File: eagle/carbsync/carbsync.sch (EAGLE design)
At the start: 27 parts, among them Q1 IRLML6344

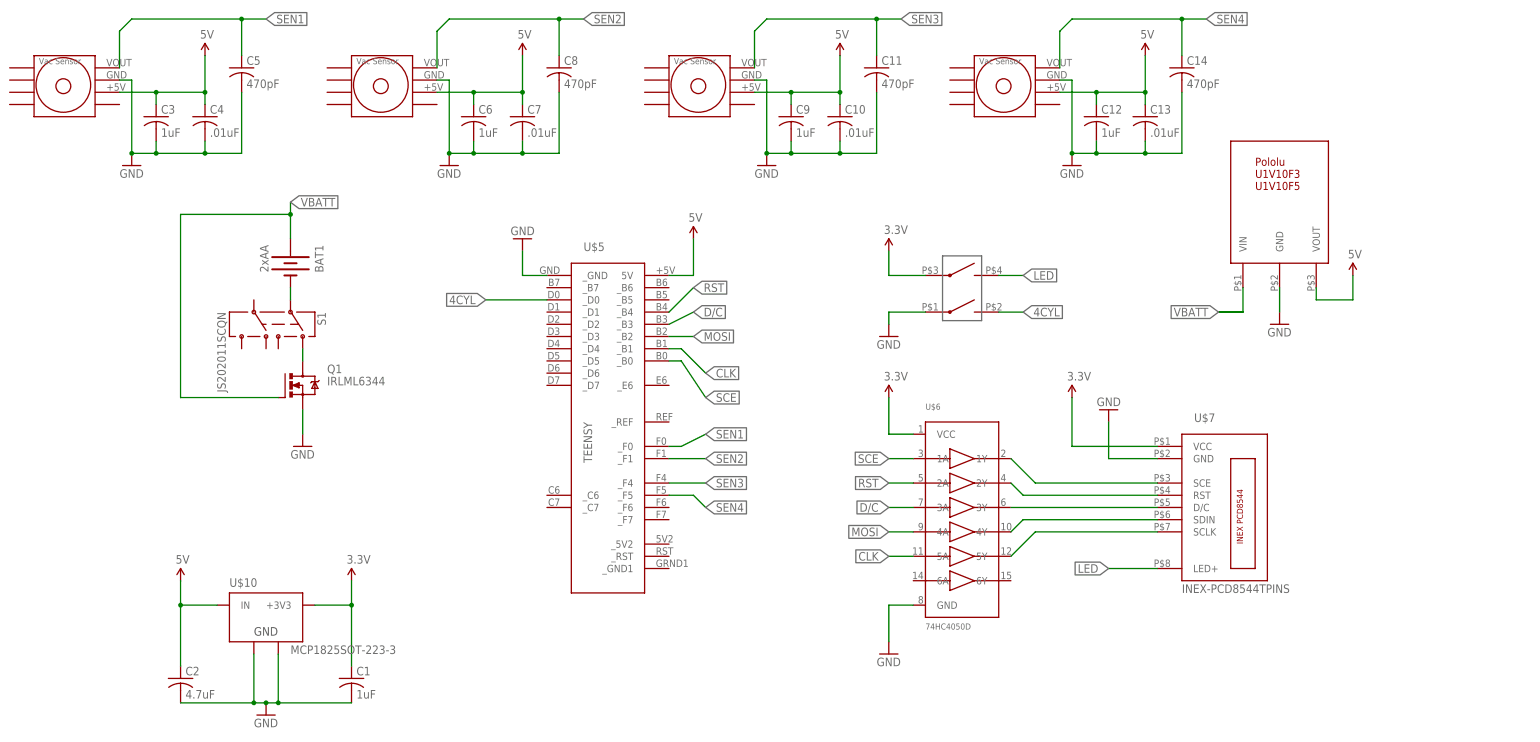
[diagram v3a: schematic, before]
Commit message: redesign PCB around http://www.hammondmfg.com/pdf/1553D_BAT.pdf
still need to find a power switch which will work correctly
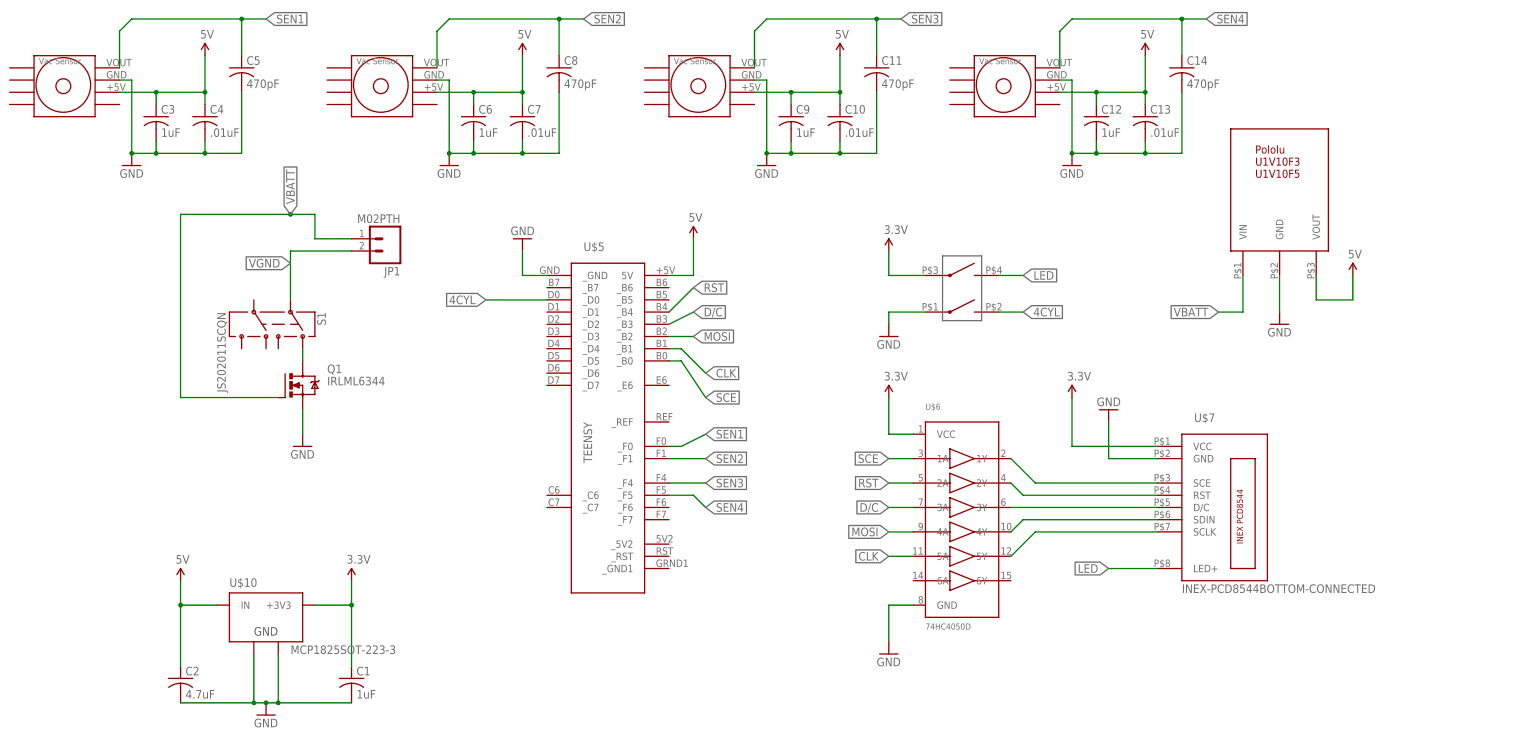
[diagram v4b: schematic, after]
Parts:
- removed BAT1: 2xAA, synfinatic:BATTERYKEYSTONE-2462-2-AA
- added JP1: M02PTH, SparkFun-Connectors:M02PTH
- U$7: value INEX-PCD8544TPINS -> INEX-PCD8544BOTTOM-CONNECTED; device synfinatic:INEX-PCD8544TPINS -> synfinatic:INEX-PCD8544BOTTOM-CONNECTED
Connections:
- removed net N$7: BAT1.-, S1.2
- new net VGND: JP1.2, S1.2
- net VBATT: now also JP1.1; no longer BAT1.+
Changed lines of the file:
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@@
 <layer number="111" name="LPC17xx" color="7" fill="1" visible="no" active="yes"/>
 <layer number="112" name="tSilk" color="7" fill="1" visible="no" active="yes"/>
+<layer number="113" name="IDFDebug" color="4" fill="1" visible="yes" active="yes"/>
 <layer number="116" name="Patch_BOT" color="9" fill="4" visible="no" active="yes"/>
 <layer number="121" name="_tsilk" color="7" fill="1" visible="yes" active="yes"/>
@@
 <part name="U$5" library="teensy" deviceset="TEENSY" device=""/>
 <part name="U$1" library="synfinatic" deviceset="MPXV5050V" device=""/>
-<part name="U$7" library="synfinatic" deviceset="INEX-PCD8544" device="TPINS" value="INEX-PCD8544TPINS"/>
+<part name="U$7" library="synfinatic" deviceset="INEX-PCD8544" device="BOTTOM-CONNECTED" value="INEX-PCD8544BOTTOM-CONNECTED"/>
 <part name="SUPPLY2" library="SparkFun-Aesthetics" deviceset="5V" device=""/>
 <part name="GND2" library="SparkFun-Aesthetics" deviceset="GND" device=""/>
@@
 <part name="C13" library="resistor" deviceset="C-US" device="C0805" value=".01uF"/>
 <part name="C14" library="resistor" deviceset="C-US" device="C0603" value="470pF"/>
-<part name="BAT1" library="synfinatic" deviceset="BATTERY" device="KEYSTONE-2462-2-AA" value="2xAA"/>
 <part name="U$9" library="synfinatic" deviceset="CT-219-X-MST" device=""/>
 <part name="SUPPLY10" library="SparkFun-Aesthetics" deviceset="3.3V" device=""/>
 <part name="GND12" library="SparkFun-Aesthetics" deviceset="GND" device=""/>
 <part name="Q1" library="synfinatic" deviceset="IRLML6344" device=""/>
+<part name="JP1" library="SparkFun-Connectors" deviceset="M02" device="PTH"/>
 </parts>
 <sheets>
@@
 <instance part="U$6" gate="G$1" x="111.76" y="38.1"/>
 <instance part="GND6" gate="1" x="96.52" y="10.16"/>
-<instance part="U$8" gate="G$1" x="167.64" y="91.44"/>
+<instance part="U$8" gate="G$1" x="167.64" y="93.98"/>
 <instance part="GND1" gate="1" x="177.8" y="78.74"/>
 <instance part="SUPPLY1" gate="G$1" x="193.04" y="88.9"/>
@@
 <instance part="C13" gate="G$1" x="149.86" y="121.92"/>
 <instance part="C14" gate="G$1" x="157.48" y="132.08"/>
-<instance part="BAT1" gate="G$1" x="-27.94" y="91.44" rot="R270"/>
 <instance part="U$9" gate="DIP$1" x="109.22" y="83.82"/>
 <instance part="SUPPLY10" gate="G$1" x="96.52" y="93.98"/>
 <instance part="GND12" gate="1" x="96.52" y="76.2"/>
 <instance part="Q1" gate="G$1" x="-27.94" y="66.04"/>
+<instance part="JP1" gate="G$1" x="-7.62" y="96.52" rot="R180"/>
 </instances>
 <busses>
@@
 <segment>
 <pinref part="U$8" gate="G$1" pin="GND"/>
-<wire x1="177.8" y1="86.36" x2="177.8" y2="81.28" width="0.1524" layer="91"/>
+<wire x1="177.8" y1="88.9" x2="177.8" y2="81.28" width="0.1524" layer="91"/>
 <pinref part="GND1" gate="1" pin="GND"/>
 </segment>
@@
 <segment>
 <pinref part="U$8" gate="G$1" pin="VOUT"/>
-<wire x1="185.42" y1="86.36" x2="185.42" y2="83.82" width="0.1524" layer="91"/>
+<wire x1="185.42" y1="88.9" x2="185.42" y2="83.82" width="0.1524" layer="91"/>
 <wire x1="185.42" y1="83.82" x2="193.04" y2="83.82" width="0.1524" layer="91"/>
 <wire x1="193.04" y1="83.82" x2="193.04" y2="88.9" width="0.1524" layer="91"/>
@@
 <net name="VBATT" class="0">
 <segment>
-<pinref part="U$8" gate="G$1" pin="VIN"/>
-<wire x1="170.18" y1="86.36" x2="170.18" y2="81.28" width="0.1524" layer="91"/>
-<wire x1="170.18" y1="81.28" x2="165.1" y2="81.28" width="0.1524" layer="91"/>
 <label x="165.1" y="81.28" size="1.778" layer="95" rot="R180" xref="yes"/>
 <wire x1="170.18" y1="81.28" x2="165.1" y2="81.28" width="0.1524" layer="91"/>
-</segment>
-<segment>
-<pinref part="BAT1" gate="G$1" pin="+"/>
-<wire x1="-27.94" y1="104.14" x2="-27.94" y2="101.6" width="0.1524" layer="91"/>
-<label x="-27.94" y="104.14" size="1.778" layer="95" xref="yes"/>
+<pinref part="U$8" gate="G$1" pin="VIN"/>
+<wire x1="170.18" y1="81.28" x2="170.18" y2="88.9" width="0.1524" layer="91"/>
+</segment>
+<segment>
+<label x="-27.94" y="101.6" size="1.778" layer="95" rot="R90" xref="yes"/>
 <pinref part="Q1" gate="G$1" pin="G"/>
-<wire x1="-27.94" y1="101.6" x2="-27.94" y2="96.52" width="0.1524" layer="91"/>
 <wire x1="-30.48" y1="63.5" x2="-50.8" y2="63.5" width="0.1524" layer="91"/>
 <wire x1="-50.8" y1="63.5" x2="-50.8" y2="101.6" width="0.1524" layer="91"/>
 <wire x1="-50.8" y1="101.6" x2="-27.94" y2="101.6" width="0.1524" layer="91"/>
+<wire x1="-27.94" y1="101.6" x2="-22.86" y2="101.6" width="0.1524" layer="91"/>
 <junction x="-27.94" y="101.6"/>
+<wire x1="-22.86" y1="101.6" x2="-22.86" y2="96.52" width="0.1524" layer="91"/>
+<pinref part="JP1" gate="G$1" pin="1"/>
+<wire x1="-15.24" y1="96.52" x2="-22.86" y2="96.52" width="0.1524" layer="91"/>
 </segment>
 </net>
@@
 </segment>
 </net>
-<net name="N$7" class="0">
-<segment>
-<pinref part="BAT1" gate="G$1" pin="-"/>
+<net name="VGND" class="0">
+<segment>
 <pinref part="S1" gate="G$1" pin="2"/>
-<wire x1="-27.94" y1="86.36" x2="-27.94" y2="83.82" width="0.1524" layer="91"/>
-</segment>
-</net>
+<wire x1="-27.94" y1="93.98" x2="-27.94" y2="83.82" width="0.1524" layer="91"/>
+<label x="-27.94" y="91.44" size="1.778" layer="95" rot="R180" xref="yes"/>
+<pinref part="JP1" gate="G$1" pin="2"/>
+<wire x1="-15.24" y1="93.98" x2="-27.94" y2="93.98" width="0.1524" layer="91"/>
+</segment>
+</net>

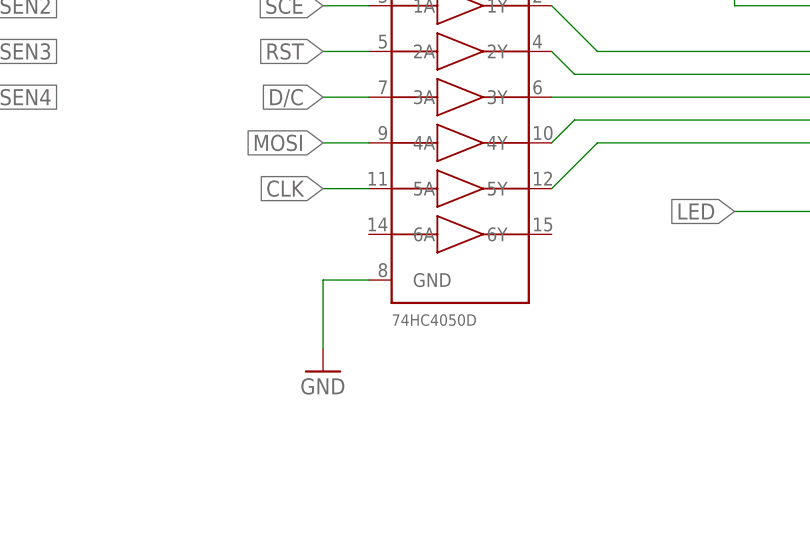
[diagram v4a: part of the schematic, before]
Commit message: clean up board and fix the level shifter
Waiting on part order to check footprints & do power switch
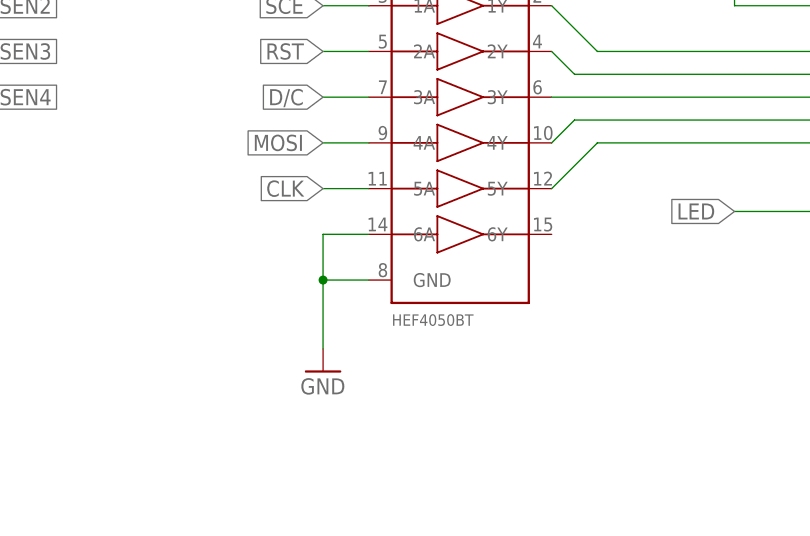
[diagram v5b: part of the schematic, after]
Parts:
- U$6: value 74HC4050D -> HEF4050BT
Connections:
- net GND: now also U$6.6A
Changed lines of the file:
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@@
 <part name="GND4" library="SparkFun-Aesthetics" deviceset="GND" device=""/>
 <part name="SUPPLY5" library="SparkFun-Aesthetics" deviceset="5V" device=""/>
-<part name="U$6" library="microbuilder" deviceset="74HC4050D" device="" value="74HC4050D"/>
+<part name="U$6" library="microbuilder" deviceset="74HC4050D" device="" value="HEF4050BT"/>
 <part name="GND6" library="SparkFun-Aesthetics" deviceset="GND" device=""/>
 <part name="U$8" library="synfinatic" deviceset="POLOLU-DC-3PIN" device="U1V10F5-5V-DC-UP"/>
@@
 <wire x1="96.52" y1="20.32" x2="96.52" y2="12.7" width="0.1524" layer="91"/>
 <pinref part="GND6" gate="1" pin="GND"/>
+<pinref part="U$6" gate="G$1" pin="6A"/>
+<wire x1="101.6" y1="25.4" x2="96.52" y2="25.4" width="0.1524" layer="91"/>
+<wire x1="96.52" y1="25.4" x2="96.52" y2="20.32" width="0.1524" layer="91"/>
+<junction x="96.52" y="20.32"/>
 </segment>
 <segment>

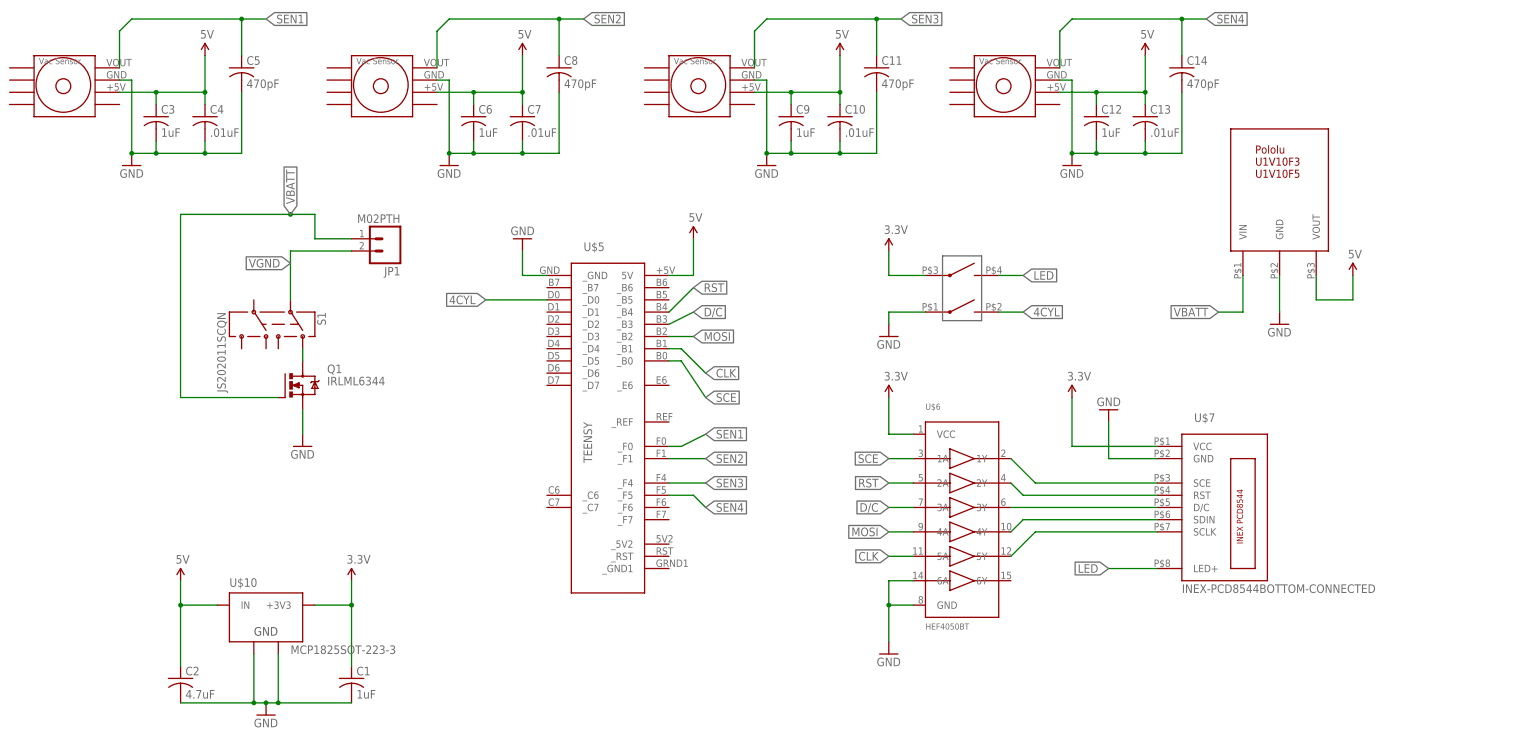
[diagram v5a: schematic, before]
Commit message: v1.0 of PCB done and ordered
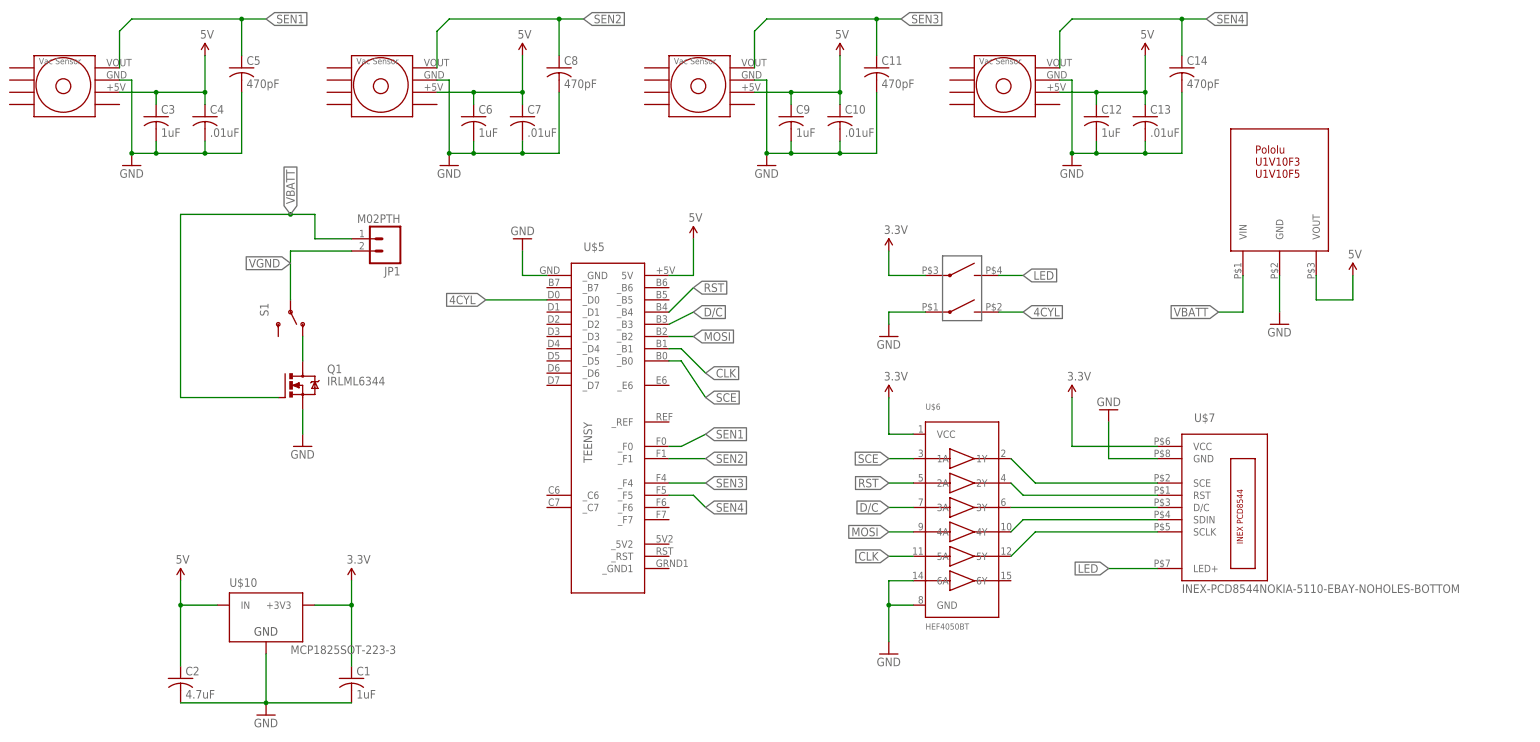
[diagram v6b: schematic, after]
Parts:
- S1: value JS202011SCQN -> (none); device synfinatic:SWITCH-DPDTC&K-JS202011SCQN -> synfinatic:SWITCH-SPDT
- U$7: value INEX-PCD8544BOTTOM-CONNECTED -> INEX-PCD8544NOKIA-5110-EBAY-NOHOLES-BOTTOM; device synfinatic:INEX-PCD8544BOTTOM-CONNECTED -> synfinatic:INEX-PCD8544NOKIA-5110-EBAY-NOHOLES-BOTTOM
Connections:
- net GND: now also U$10.GND; no longer U$10.GND@1, U$10.GND@2
- net N$6: now also S1.O; no longer S1.1
- net VGND: now also S1.P; no longer S1.2
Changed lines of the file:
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@@
 <part name="U$5" library="teensy" deviceset="TEENSY" device=""/>
 <part name="U$1" library="synfinatic" deviceset="MPXV5050V" device=""/>
-<part name="U$7" library="synfinatic" deviceset="INEX-PCD8544" device="BOTTOM-CONNECTED" value="INEX-PCD8544BOTTOM-CONNECTED"/>
+<part name="U$7" library="synfinatic" deviceset="INEX-PCD8544" device="NOKIA-5110-EBAY-NOHOLES-BOTTOM" value="INEX-PCD8544NOKIA-5110-EBAY-NOHOLES-BOTTOM"/>
 <part name="SUPPLY2" library="SparkFun-Aesthetics" deviceset="5V" device=""/>
 <part name="GND2" library="SparkFun-Aesthetics" deviceset="GND" device=""/>
@@
 <part name="SUPPLY7" library="SparkFun-Aesthetics" deviceset="3.3V" device=""/>
 <part name="SUPPLY13" library="SparkFun-Aesthetics" deviceset="3.3V" device=""/>
-<part name="S1" library="synfinatic" deviceset="SWITCH-DPDT" device="C&amp;K-JS202011SCQN" value="JS202011SCQN"/>
 <part name="C3" library="resistor" deviceset="C-US" device="C0805" value="1uF"/>
 <part name="C4" library="resistor" deviceset="C-US" device="C0805" value=".01uF"/>
@@
 <part name="Q1" library="synfinatic" deviceset="IRLML6344" device=""/>
 <part name="JP1" library="SparkFun-Connectors" deviceset="M02" device="PTH"/>
+<part name="S1" library="synfinatic" deviceset="SWITCH-SPDT" device=""/>
 </parts>
 <sheets>
@@
 <instance part="SUPPLY7" gate="G$1" x="134.62" y="63.5"/>
 <instance part="SUPPLY13" gate="G$1" x="96.52" y="63.5"/>
-<instance part="S1" gate="G$1" x="-30.48" y="78.74" rot="R270"/>
 <instance part="C3" gate="G$1" x="-55.88" y="121.92"/>
 <instance part="C4" gate="G$1" x="-45.72" y="121.92"/>
@@
 <instance part="Q1" gate="G$1" x="-27.94" y="66.04"/>
 <instance part="JP1" gate="G$1" x="-7.62" y="96.52" rot="R180"/>
+<instance part="S1" gate="1" x="-27.94" y="81.28" rot="R270"/>
 </instances>
 <busses>
@@
 <segment>
 <pinref part="C2" gate="G$1" pin="2"/>
-<wire x1="-50.8" y1="0" x2="-35.56" y2="0" width="0.1524" layer="91"/>
-<wire x1="-35.56" y1="0" x2="-33.02" y2="0" width="0.1524" layer="91"/>
-<wire x1="-33.02" y1="0" x2="-30.48" y2="0" width="0.1524" layer="91"/>
+<wire x1="-50.8" y1="0" x2="-33.02" y2="0" width="0.1524" layer="91"/>
 <pinref part="C1" gate="G$1" pin="2"/>
 <junction x="-33.02" y="0"/>
 <pinref part="GND11" gate="1" pin="GND"/>
-<pinref part="U$10" gate="G$1" pin="GND@1"/>
-<wire x1="-30.48" y1="0" x2="-15.24" y2="0" width="0.1524" layer="91"/>
-<wire x1="-35.56" y1="10.16" x2="-35.56" y2="0" width="0.1524" layer="91"/>
-<junction x="-35.56" y="0"/>
-<pinref part="U$10" gate="G$1" pin="GND@2"/>
-<wire x1="-30.48" y1="10.16" x2="-30.48" y2="0" width="0.1524" layer="91"/>
-<junction x="-30.48" y="0"/>
+<wire x1="-33.02" y1="0" x2="-15.24" y2="0" width="0.1524" layer="91"/>
+<pinref part="U$10" gate="G$1" pin="GND"/>
+<wire x1="-33.02" y1="10.16" x2="-33.02" y2="0" width="0.1524" layer="91"/>
 </segment>
 <segment>
@@
 <net name="VGND" class="0">
 <segment>
-<pinref part="S1" gate="G$1" pin="2"/>
 <wire x1="-27.94" y1="93.98" x2="-27.94" y2="83.82" width="0.1524" layer="91"/>
 <label x="-27.94" y="91.44" size="1.778" layer="95" rot="R180" xref="yes"/>
 <pinref part="JP1" gate="G$1" pin="2"/>
 <wire x1="-15.24" y1="93.98" x2="-27.94" y2="93.98" width="0.1524" layer="91"/>
+<pinref part="S1" gate="1" pin="P"/>
 </segment>
 </net>
@@
 <net name="N$6" class="0">
 <segment>
-<pinref part="S1" gate="G$1" pin="1"/>
 <pinref part="Q1" gate="G$1" pin="D"/>
-<wire x1="-25.4" y1="73.66" x2="-25.4" y2="71.12" width="0.1524" layer="91"/>
-</segment>
-</net>
+<wire x1="-25.4" y1="76.2" x2="-25.4" y2="71.12" width="0.1524" layer="91"/>
+<pinref part="S1" gate="1" pin="O"/>
+</segment>
+</net>
